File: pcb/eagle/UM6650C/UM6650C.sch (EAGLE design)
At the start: 11 parts, among them U1 74HC139, U2 74HC00, U3 74HC373, U4 28C64AVS

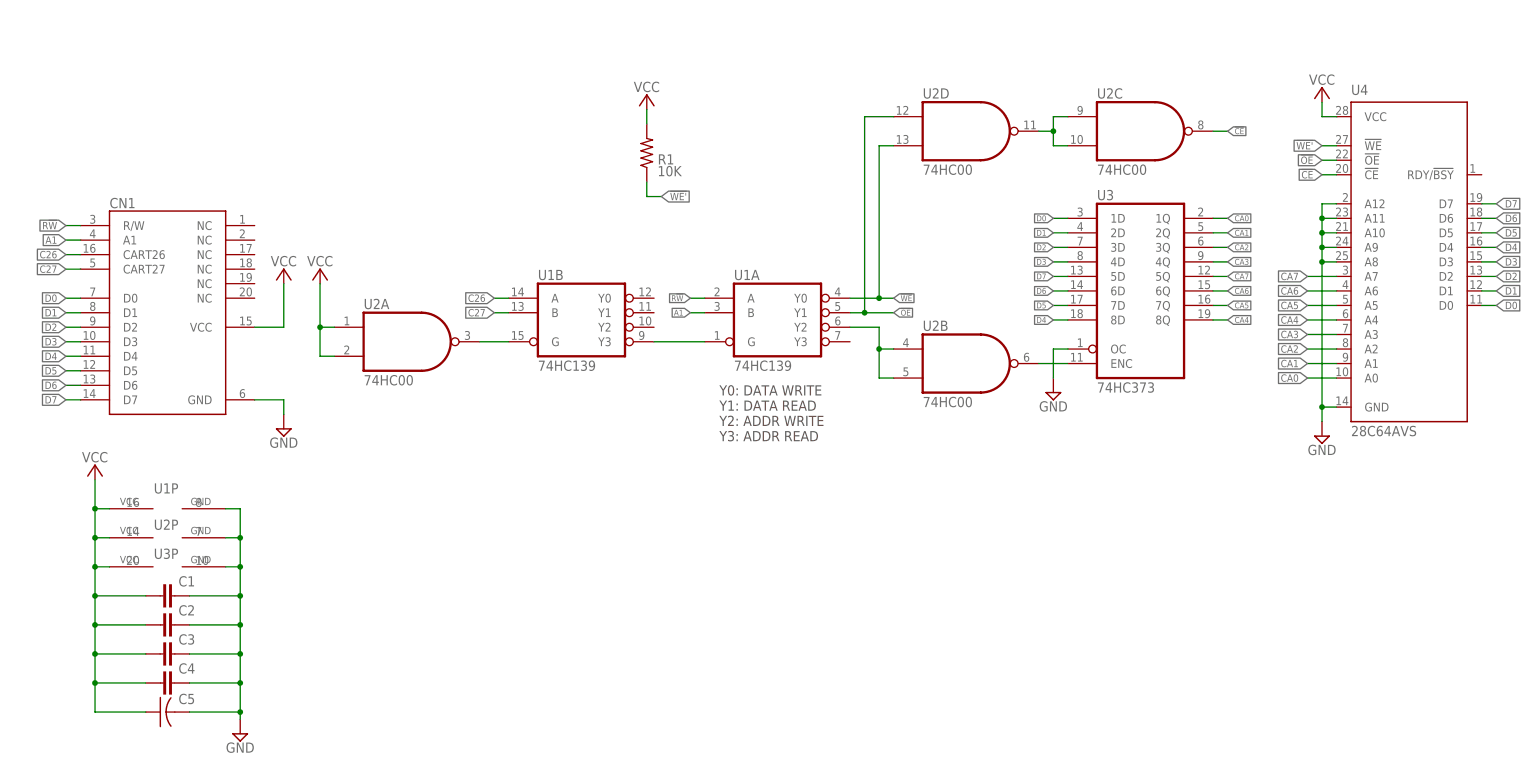
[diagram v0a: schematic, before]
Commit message: Add Multitap schematic and board file
Update UM6650C board file
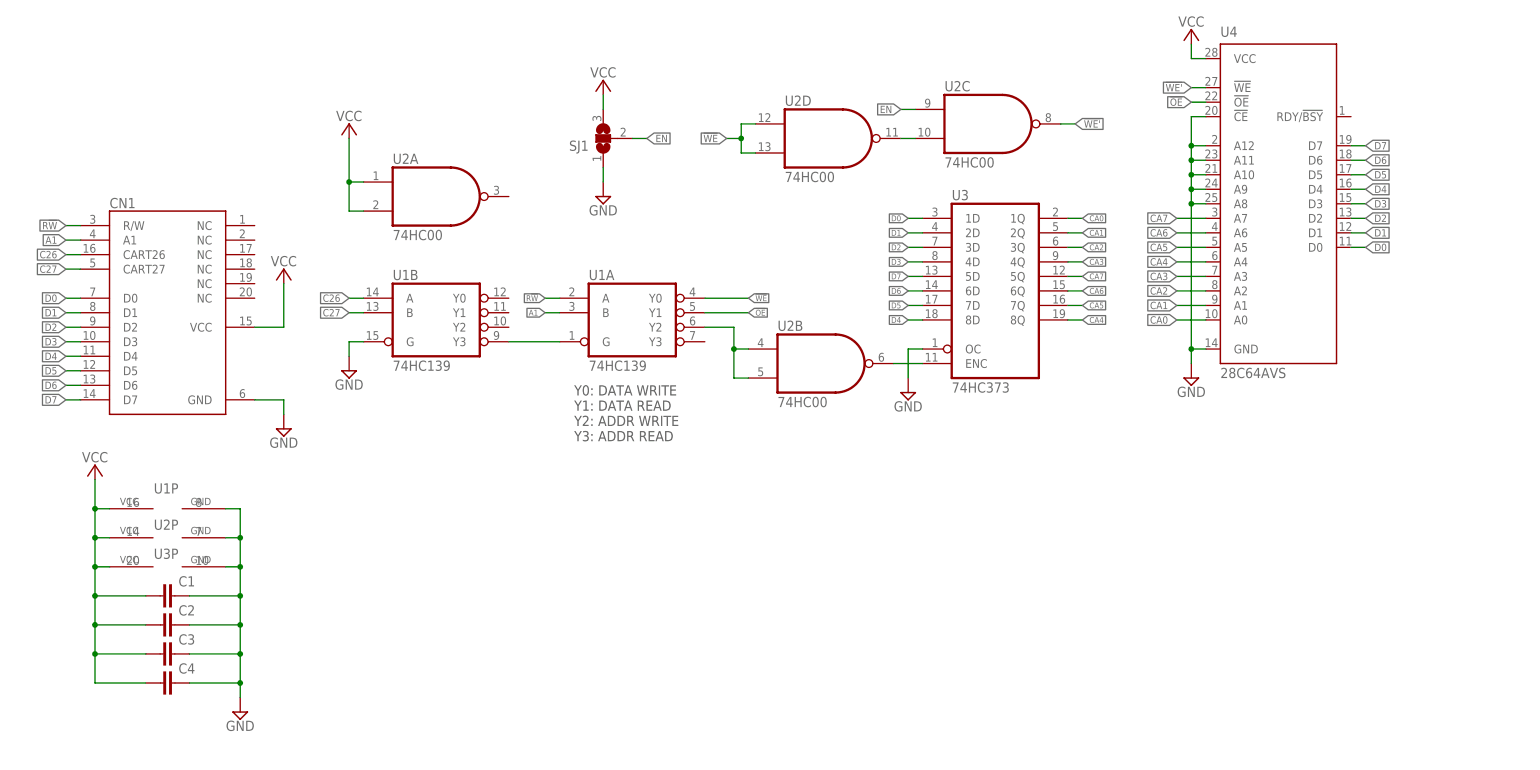
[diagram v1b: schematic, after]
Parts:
- removed C5: (no value), rcl:C-USC1210
- removed R1: 10K, rcl:R-US_R0603
- added SJ1: (no value), jumper:SJ2W
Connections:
- removed net !CE: U2C.O, U4.!CE
- removed net N$4: U1B.G, U2A.O
- new net EN: SJ1.2, U2C.I0
- net !OE: no longer U2D.I0
- net !WE: now also U2D.I0
- net !WE': now also U2C.O; no longer R1.1
- net GND: now also SJ1.1, U1B.G, U4.!CE; no longer C5.2
- net N$1: no longer U2C.I0
- net VCC: now also SJ1.3; no longer C5.1, R1.2
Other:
- moved on the sheet: U1A, U1B, U2A, U2B, U2C, U2D, U3, U4
